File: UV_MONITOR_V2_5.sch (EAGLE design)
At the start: 33 parts, among them U2 LM2903M, U3 MCP7940N-I/SN, U4 ML8511 UV_SENSOR, U9 MIC5219 3.3V, Y1 32.768kHz

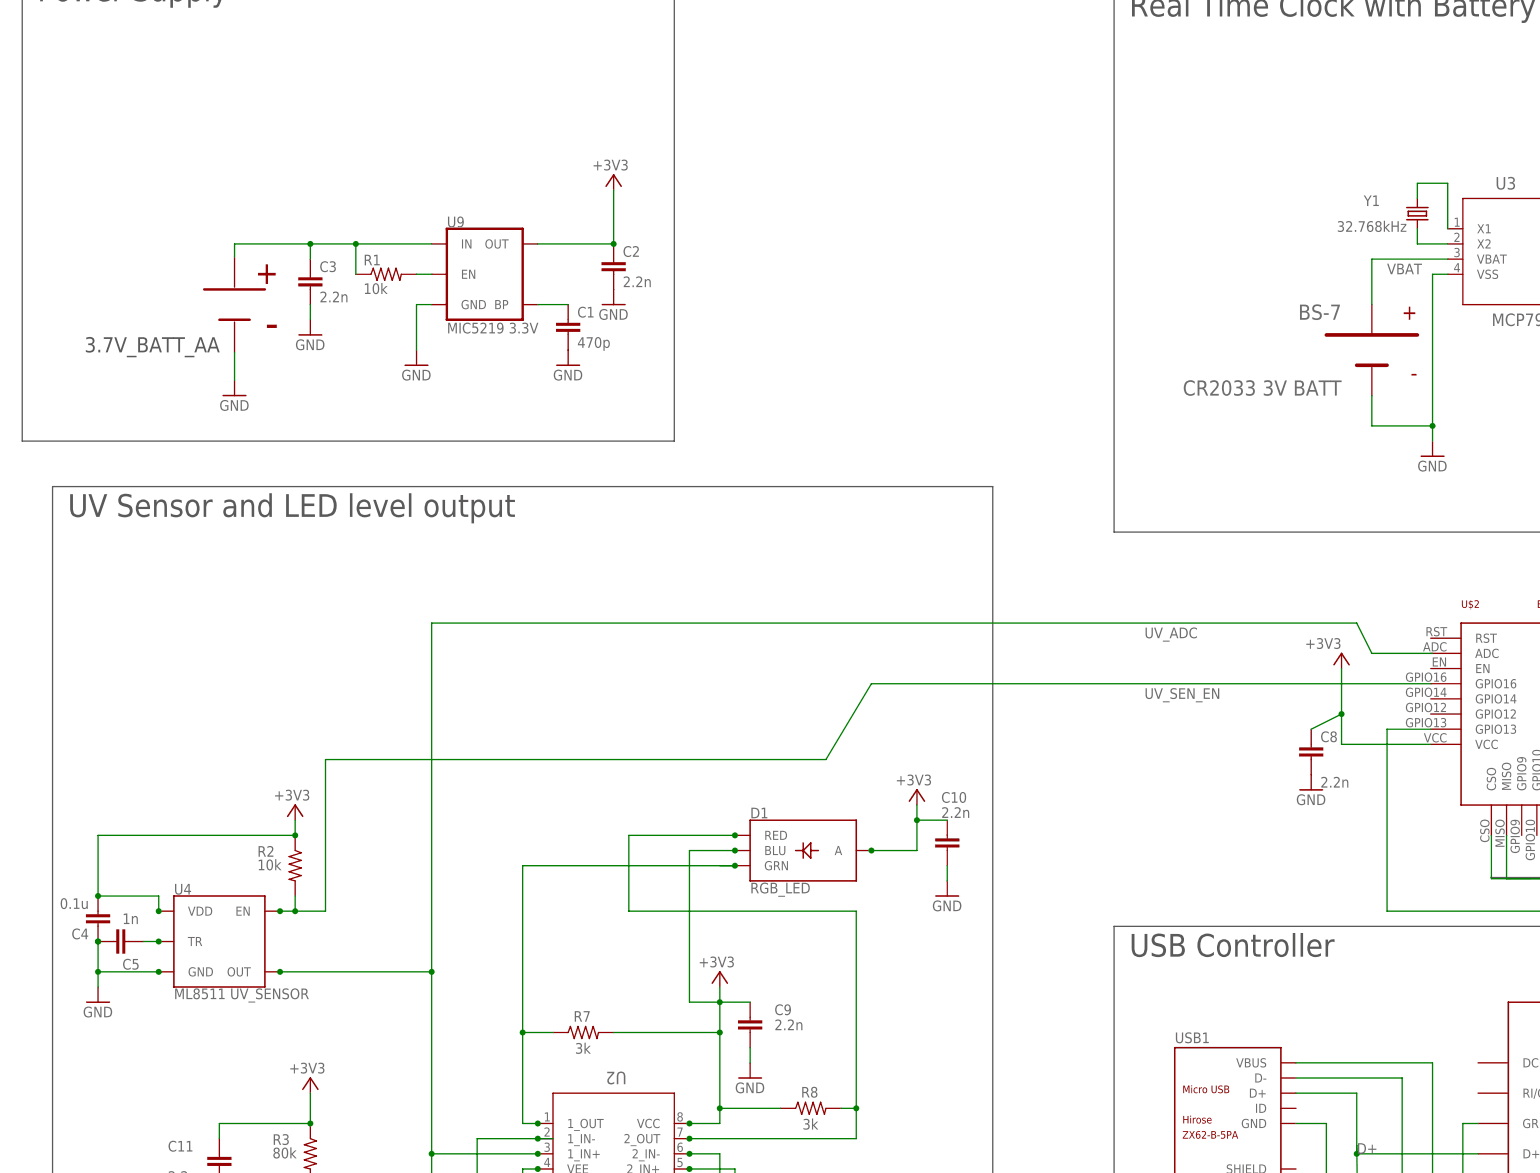
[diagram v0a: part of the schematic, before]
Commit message: minor edits
Created some edits for my own benefit. These edits were to an old version of our schematic and board.
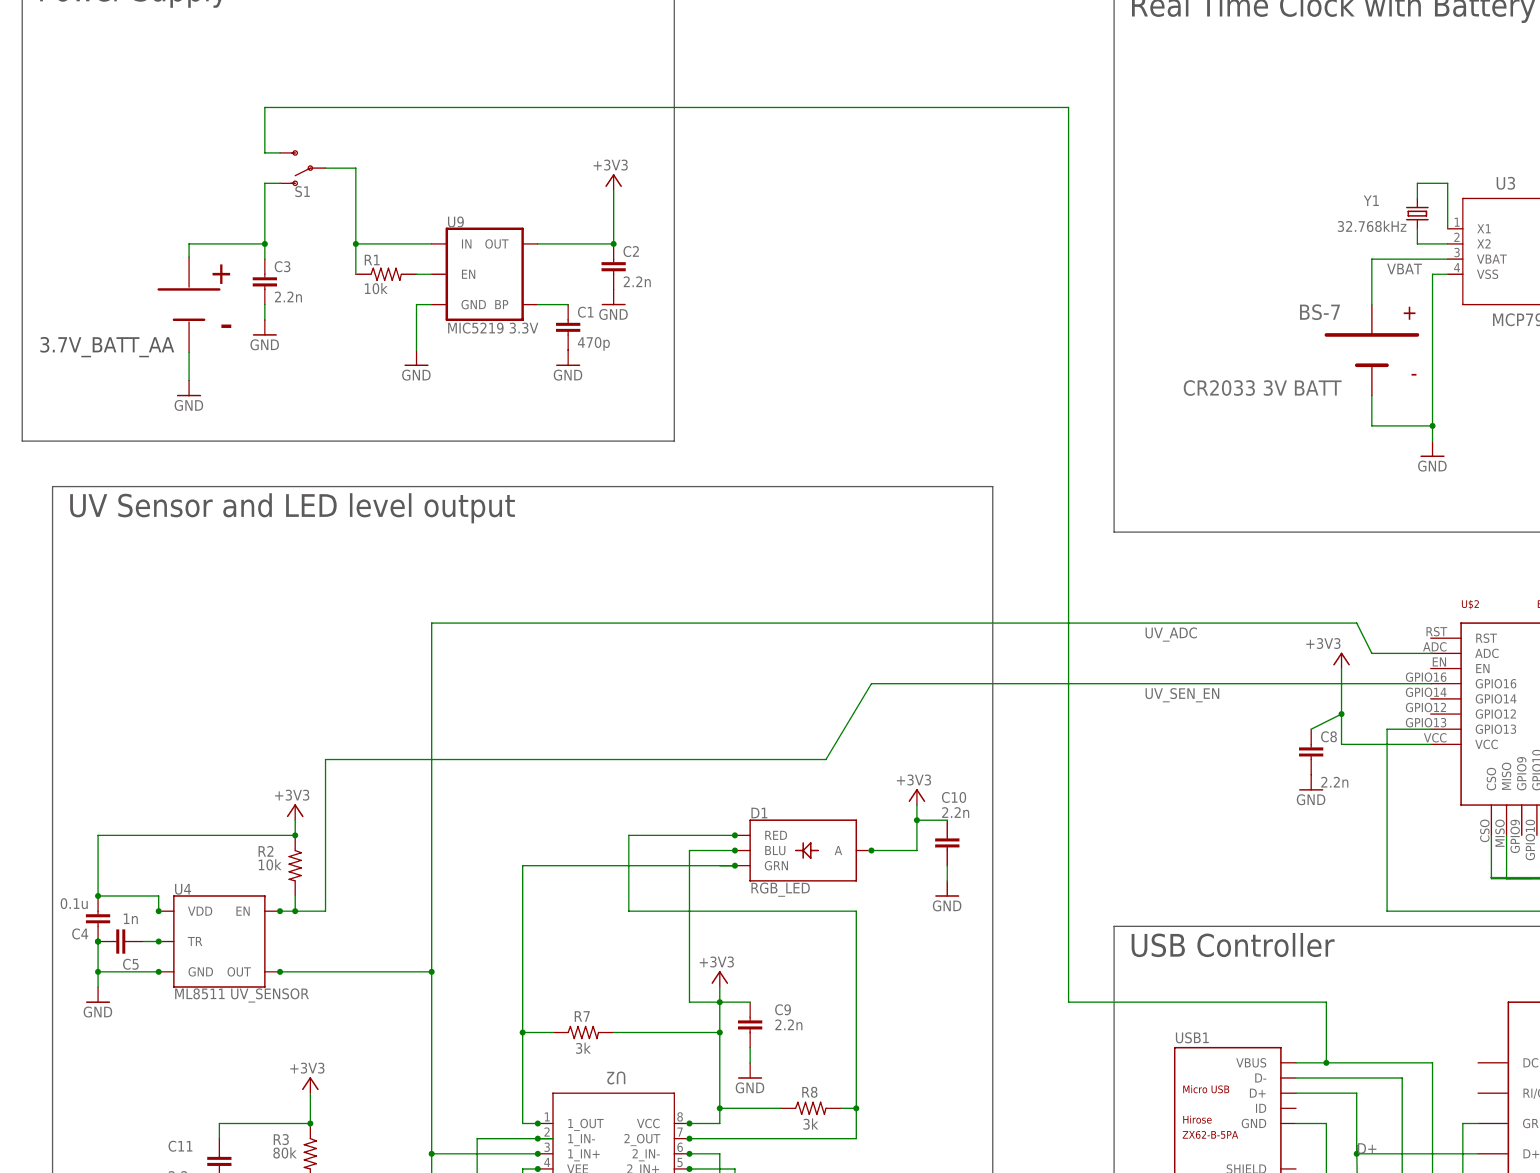
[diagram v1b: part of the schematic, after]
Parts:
- added S1: (no value), SparkFun-Switches:SWITCH-SPDT-SMD-RIGHT-ANGLE
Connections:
- new net N$11: C3.1, S1.O, U$3.VBAT
- net MAIN_BAT: now also S1.P; no longer C3.1, U$3.VBAT
- net VBUS: now also S1.S
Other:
- moved on the sheet: C3
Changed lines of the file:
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@@
 <part name="GND14" library="supply1" library_urn="urn:adsk.eagle:library:371" deviceset="GND" device=""/>
 <part name="GND22" library="supply1" library_urn="urn:adsk.eagle:library:371" deviceset="GND" device=""/>
+<part name="S1" library="SparkFun-Switches" library_urn="urn:adsk.eagle:library:535" deviceset="SWITCH-SPDT" device="-SMD-RIGHT-ANGLE" package3d_urn="urn:adsk.eagle:package:40179/1"/>
 </parts>
 <sheets>
@@
 <instance part="C1" gate="G$1" x="99.06" y="210.82"/>
 <instance part="C2" gate="G$1" x="106.68" y="220.98"/>
-<instance part="C3" gate="G$1" x="55.88" y="218.44" smashed="yes">
-<attribute name="NAME" x="57.404" y="218.821" size="1.778" layer="95"/>
-<attribute name="VALUE" x="57.404" y="213.741" size="1.778" layer="96"/>
+<instance part="C3" gate="G$1" x="48.26" y="218.44" smashed="yes">
+<attribute name="NAME" x="49.784" y="218.821" size="1.778" layer="95"/>
+<attribute name="VALUE" x="49.784" y="213.741" size="1.778" layer="96"/>
 </instance>
 <instance part="R1" gate="G$1" x="68.58" y="218.44"/>
-<instance part="GND7" gate="1" x="55.88" y="208.28"/>
+<instance part="GND7" gate="1" x="48.26" y="208.28"/>
 <instance part="GND8" gate="1" x="106.68" y="213.36"/>
-<instance part="GND9" gate="1" x="43.18" y="198.12"/>
+<instance part="GND9" gate="1" x="35.56" y="198.12"/>
 <instance part="C4" gate="G$1" x="20.32" y="109.22" rot="R180"/>
 <instance part="C5" gate="G$1" x="25.4" y="106.68" smashed="yes" rot="R270">
@@
 <attribute name="VALUE" x="285.242" y="227.33" size="1.778" layer="96" rot="R90"/>
 </instance>
-<instance part="U$3" gate="G$1" x="43.18" y="213.36" smashed="yes" rot="MR0"/>
+<instance part="U$3" gate="G$1" x="35.56" y="213.36" smashed="yes" rot="MR0"/>
 <instance part="U$4" gate="G$1" x="233.68" y="205.74" smashed="yes" rot="MR0">
 <attribute name="VALUE" x="228.6" y="210.82" size="2.54" layer="96" rot="MR0"/>
@@
 <instance part="GND14" gate="1" x="223.52" y="25.4"/>
 <instance part="GND22" gate="1" x="248.92" y="40.64"/>
+<instance part="S1" gate="1" x="55.88" y="236.22" rot="R180"/>
 </instances>
 <busses>
@@
 <pinref part="C3" gate="G$1" pin="2"/>
 <pinref part="GND7" gate="1" pin="GND"/>
-<wire x1="55.88" y1="213.36" x2="55.88" y2="210.82" width="0.1524" layer="91"/>
+<wire x1="48.26" y1="213.36" x2="48.26" y2="210.82" width="0.1524" layer="91"/>
 </segment>
 <segment>
@@
 <segment>
 <pinref part="GND9" gate="1" pin="GND"/>
-<wire x1="43.18" y1="200.66" x2="43.18" y2="205.36" width="0.1524" layer="91"/>
+<wire x1="35.56" y1="200.66" x2="35.56" y2="205.36" width="0.1524" layer="91"/>
 <pinref part="U$3" gate="G$1" pin="P$2"/>
 </segment>
@@
 <net name="MAIN_BAT" class="0">
 <segment>
-<pinref part="C3" gate="G$1" pin="1"/>
-<wire x1="55.88" y1="223.52" x2="55.88" y2="220.98" width="0.1524" layer="91"/>
 <pinref part="R1" gate="G$1" pin="1"/>
 <wire x1="63.5" y1="223.52" x2="76.2" y2="223.52" width="0.1524" layer="91"/>
 <wire x1="63.5" y1="218.44" x2="63.5" y2="223.52" width="0.1524" layer="91"/>
-<wire x1="43.18" y1="223.52" x2="55.88" y2="223.52" width="0.1524" layer="91"/>
-<junction x="55.88" y="223.52"/>
-<wire x1="55.88" y1="223.52" x2="63.5" y2="223.52" width="0.1524" layer="91"/>
+<pinref part="U9" gate="G$1" pin="IN"/>
+<pinref part="S1" gate="1" pin="P"/>
+<wire x1="58.42" y1="236.22" x2="63.5" y2="236.22" width="0.1524" layer="91"/>
+<wire x1="63.5" y1="236.22" x2="63.5" y2="223.52" width="0.1524" layer="91"/>
 <junction x="63.5" y="223.52"/>
-<pinref part="U9" gate="G$1" pin="IN"/>
-<wire x1="43.18" y1="223.52" x2="43.18" y2="221.36" width="0.1524" layer="91"/>
-<pinref part="U$3" gate="G$1" pin="VBAT"/>
 </segment>
 </net>
@@
 <segment>
 <pinref part="USB1" gate="G$1" pin="VBUS"/>
-<wire x1="220.98" y1="86.36" x2="243.84" y2="86.36" width="0.1524" layer="91"/>
+<wire x1="220.98" y1="86.36" x2="226.06" y2="86.36" width="0.1524" layer="91"/>
+<wire x1="226.06" y1="86.36" x2="243.84" y2="86.36" width="0.1524" layer="91"/>
 <wire x1="243.84" y1="86.36" x2="243.84" y2="55.88" width="0.1524" layer="91"/>
 <pinref part="U$1" gate="G$1" pin="VBUS"/>
@@
 <wire x1="221.56" y1="48.26" x2="221.56" y2="44.56" width="0.1524" layer="91"/>
 <junction x="243.84" y="48.26"/>
+<wire x1="226.06" y1="86.36" x2="226.06" y2="96.52" width="0.1524" layer="91"/>
+<junction x="226.06" y="86.36"/>
+<wire x1="226.06" y1="96.52" x2="182.88" y2="96.52" width="0.1524" layer="91"/>
+<wire x1="182.88" y1="96.52" x2="182.88" y2="246.38" width="0.1524" layer="91"/>
+<wire x1="182.88" y1="246.38" x2="48.26" y2="246.38" width="0.1524" layer="91"/>
+<wire x1="48.26" y1="246.38" x2="48.26" y2="238.76" width="0.1524" layer="91"/>
+<pinref part="S1" gate="1" pin="S"/>
+<wire x1="48.26" y1="238.76" x2="50.8" y2="238.76" width="0.1524" layer="91"/>
 </segment>
 </net>
@@
 </segment>
 </net>
+<net name="N$11" class="0">
+<segment>
+<pinref part="C3" gate="G$1" pin="1"/>
+<wire x1="48.26" y1="223.52" x2="48.26" y2="220.98" width="0.1524" layer="91"/>
+<wire x1="35.56" y1="223.52" x2="48.26" y2="223.52" width="0.1524" layer="91"/>
+<wire x1="35.56" y1="223.52" x2="35.56" y2="221.36" width="0.1524" layer="91"/>
+<pinref part="U$3" gate="G$1" pin="VBAT"/>
+<pinref part="S1" gate="1" pin="O"/>
+<wire x1="50.8" y1="233.68" x2="48.26" y2="233.68" width="0.1524" layer="91"/>
+<wire x1="48.26" y1="233.68" x2="48.26" y2="223.52" width="0.1524" layer="91"/>
+<junction x="48.26" y="223.52"/>
+</segment>
+</net>
